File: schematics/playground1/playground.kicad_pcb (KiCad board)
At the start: 2 copper layers, 60 parts, among them J1 Conn_01x05, J2 Conn_02x03_Odd_Even, J3 Conn_01x03, J4 Conn_02x04_Odd_Even, SW1 SW_SPST, SW2 SW_Push, SW3 SW_Push, U1 ADS1299, U2 MCP1700x-330xxTT, U3 PIC32MX250F128B_I_SS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

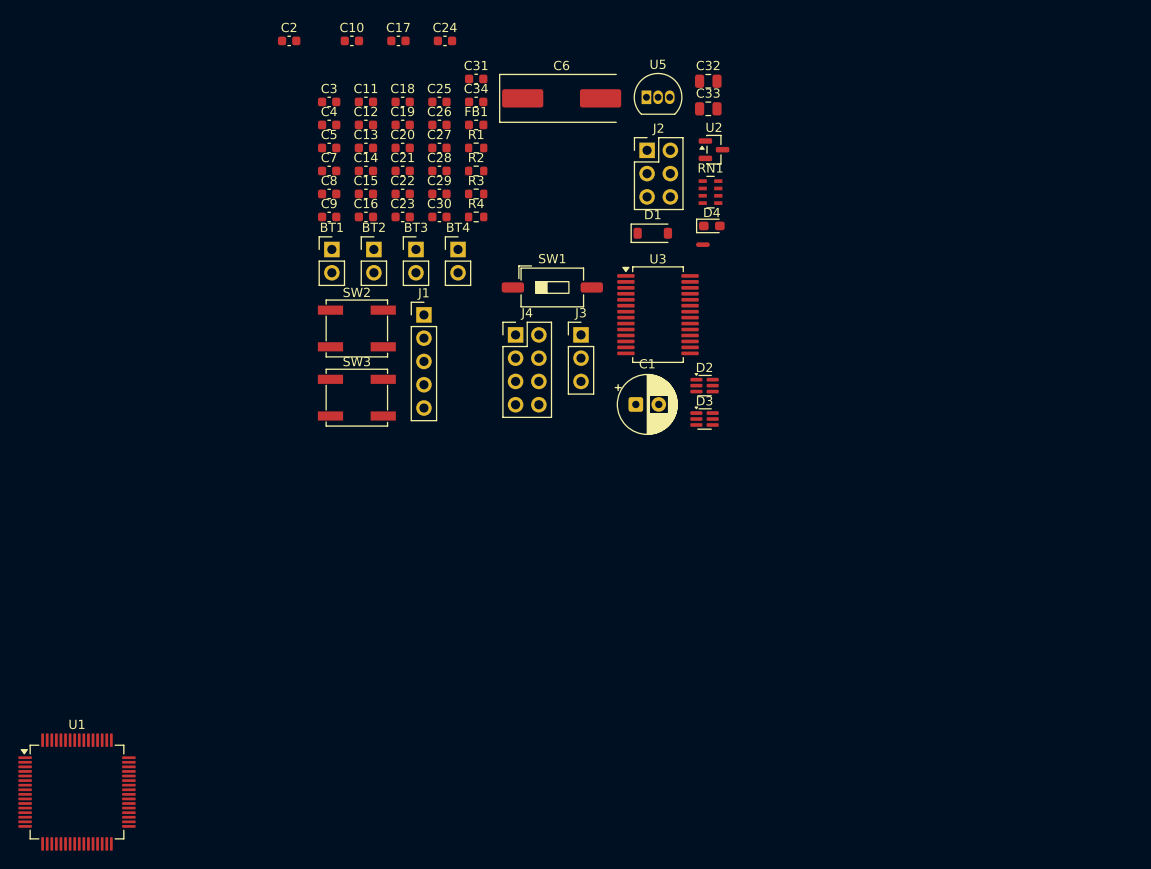
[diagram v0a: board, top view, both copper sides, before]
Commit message: alternate pcb layout
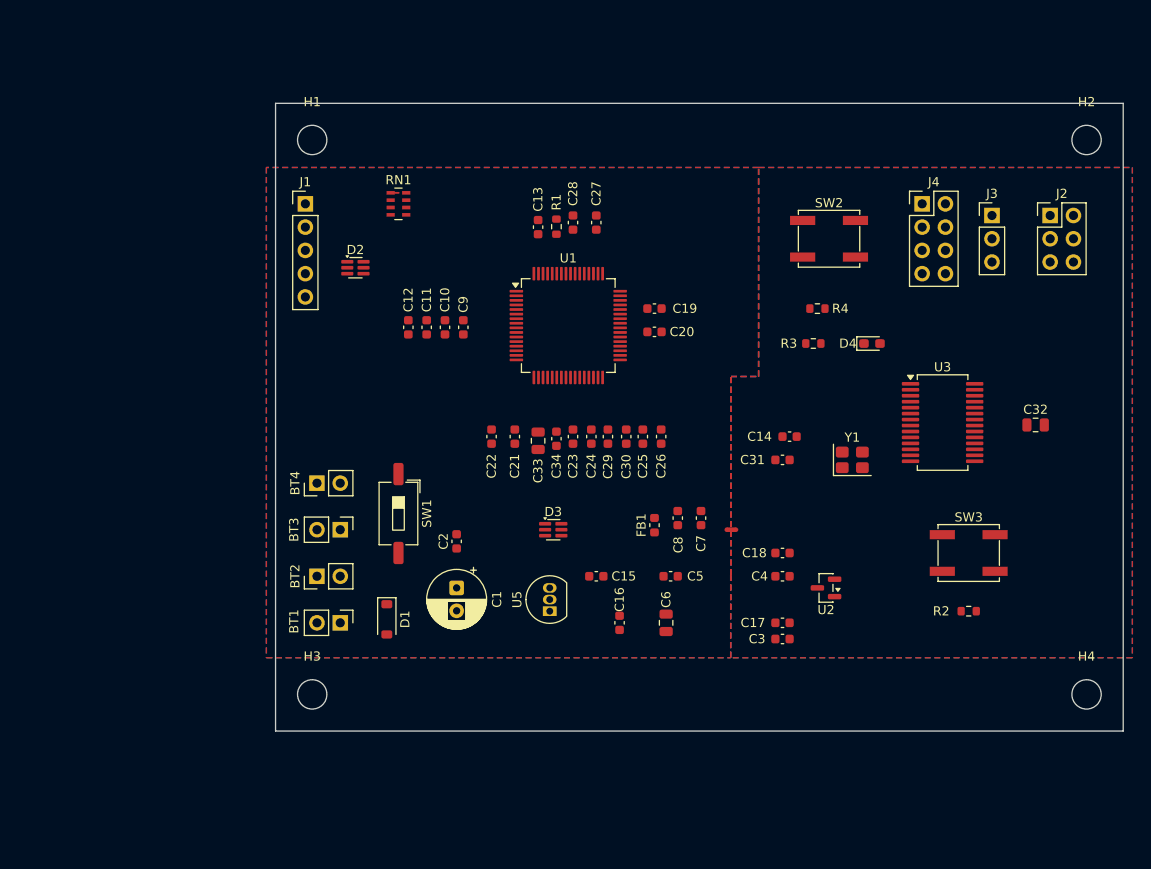
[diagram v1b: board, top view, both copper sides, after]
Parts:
- added H1: MountingHole, MountingHole:MountingHole_3.2mm_M3, F.Cu at (96.0, 70.5)
- added H2: MountingHole, MountingHole:MountingHole_3.2mm_M3, F.Cu at (180.5, 70.5)
- added H3: MountingHole, MountingHole:MountingHole_3.2mm_M3, F.Cu at (96.0, 131.0)
- added H4: MountingHole, MountingHole:MountingHole_3.2mm_M3, F.Cu at (180.5, 131.0)
- added Y1: 8MHz, Crystal:Crystal_SMD_3225-4Pin_3.2x2.5mm, F.Cu at (154.9, 105.4)
- C6: footprint Crystal:Crystal_SMD_HC49-SD -> Capacitor_SMD:C_0805_2012Metric
- moved C3 76.7 mm to (147.3, 125.0), turned to 180 degrees
- moved C17 76.1 mm to (147.3, 123.2), turned to 180 degrees
- moved U1 73.9 mm to (123.9, 90.8)
- moved R2 72.1 mm to (167.6, 121.9)
- moved C4 69.8 mm to (147.3, 118.1), turned to 180 degrees
- moved SW3 68.9 mm to (167.6, 115.6)
- moved C18 64.3 mm to (147.3, 115.6), turned to 180 degrees
- moved C5 59.8 mm to (135.1, 118.1)
- moved C6 58.4 mm to (134.6, 123.2), turned to 90 degrees
- moved C2 57.6 mm to (111.8, 114.3), turned to 90 degrees
- moved U5 57.1 mm to (121.9, 121.9), turned to 90 degrees
- moved C7 55.5 mm to (138.4, 111.8), turned to 90 degrees
- moved C14 54.6 mm to (148.1, 102.9)
- moved C31 53.3 mm to (147.3, 105.4)
- moved SW2 52.4 mm to (152.4, 81.3)
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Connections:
- U1 pad 15: /IN1P -> /IN1N
- U1 pad 16: /IN1N -> /IN1P
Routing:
- added copper zone on B.Cu, net /AGND
- added copper zone on F.Cu, net /AGND
- added copper zone on B.Cu, net /DGND
- added copper zone on F.Cu, net /DGND
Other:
- board outline added: 92.5 x 68.5 mm

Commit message: wiring alternate layout, agnd side
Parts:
- C6: footprint Capacitor_SMD:C_0805_2012Metric -> Crystal:Crystal_SMD_HC49-SD
- Y1: footprint Crystal:Crystal_SMD_3225-4Pin_3.2x2.5mm -> Crystal:Crystal_SMD_3215-2Pin_3.2x1.5mm
- moved C20 3.96 mm to (135.9, 88.4), turned to -90 degrees
- moved C25 1.36 mm to (133.3, 102.4), turned to -90 degrees
- moved C26 1.36 mm to (135.3, 102.4), turned to -90 degrees
- moved C23 1.27 mm to (125.7, 102.9)
- moved C24 1.27 mm to (127.7, 102.9)
- moved C33 1.27 mm to (121.9, 103.3), turned to 90 degrees
- moved C34 1.27 mm to (123.9, 103.1)
- moved C29 1.27 mm to (129.5, 102.9)
- moved C30 1.27 mm to (131.5, 102.9)
- turned C13 to -90 degrees
- turned C19 to 90 degrees
- turned R1 to -90 degrees
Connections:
- C13 pad 1: /BIAS_DRV -> /BIAS
- R1 pad 1: /BIAS_DRV -> /BIAS
- U1 pad 15: /IN1N -> /IN1P
- U1 pad 16: /IN1P -> /IN1N
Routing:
- net /AVDD_5V: track 0.00 -> 97.0 mm, vias 0 -> 2
- net /BIAS: track 0.00 -> 95.3 mm, vias 0 -> 4
- net /AVDD1_5V: track 0.00 -> 58.8 mm, vias 0 -> 2
- net /_SRB2: track 0.00 -> 53.6 mm, vias 0 -> 2
- net /VBAT_PROT: track 0.00 -> 49.7 mm
- net /IN1N: track 0.00 -> 43.4 mm, vias 0 -> 4
- net /IN1P: track 0.00 -> 39.5 mm
- net /_SRB1: track 0.00 -> 37.2 mm
- net /DVDD_3V3: track 0.00 -> 34.9 mm
- net /SRB1: track 0.00 -> 33.8 mm
- net /AGND: track 0.00 -> 24.2 mm
- net /1N: track 0.45 -> 18.5 mm
- net Net-(U1-VREFP): track 0.00 -> 17.0 mm
- net /1P: track 0.00 -> 16.2 mm
- net Net-(U1-VCAP2): track 0.00 -> 16.1 mm
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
